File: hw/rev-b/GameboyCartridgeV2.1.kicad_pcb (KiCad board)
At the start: 6 copper layers, 52.8 x 61.2 mm, 148 parts, among them J1 USB_C_Receptacle_USB2.0, J2 Micro_SD_Card_Det2, J4 Conn_01x06, J5 CartBus, Q1 CJ2302, Q101 SIA975DJ-T1-GE3, Q102 2N7002, SW1 SW_Push, SW2 SW_Push, U1 USBLC6-2P6, U101 TPS2116DRLR, U102 TPS2553DBVR, U103 TPS63802DLAR, U104 ESP32-C3-MINI-1U-N4, U105 SN74LVC1G125DBVR, U106 SN74LVC3G34DCTR, U107 CH334P, U108 TLV3012BIDBVR, U109 TLV431BIDBZR, U2 W25Q16JVSSIQ, U3 RP2350_80QFN, U4 W956A8MBYA5I, U5 MCP79510, U6 AP2112K-3.3, U7 TXB0108PW, Y1 12MHz, Y101 12MHz 10pF 10ppm, Y2 32.768kHz

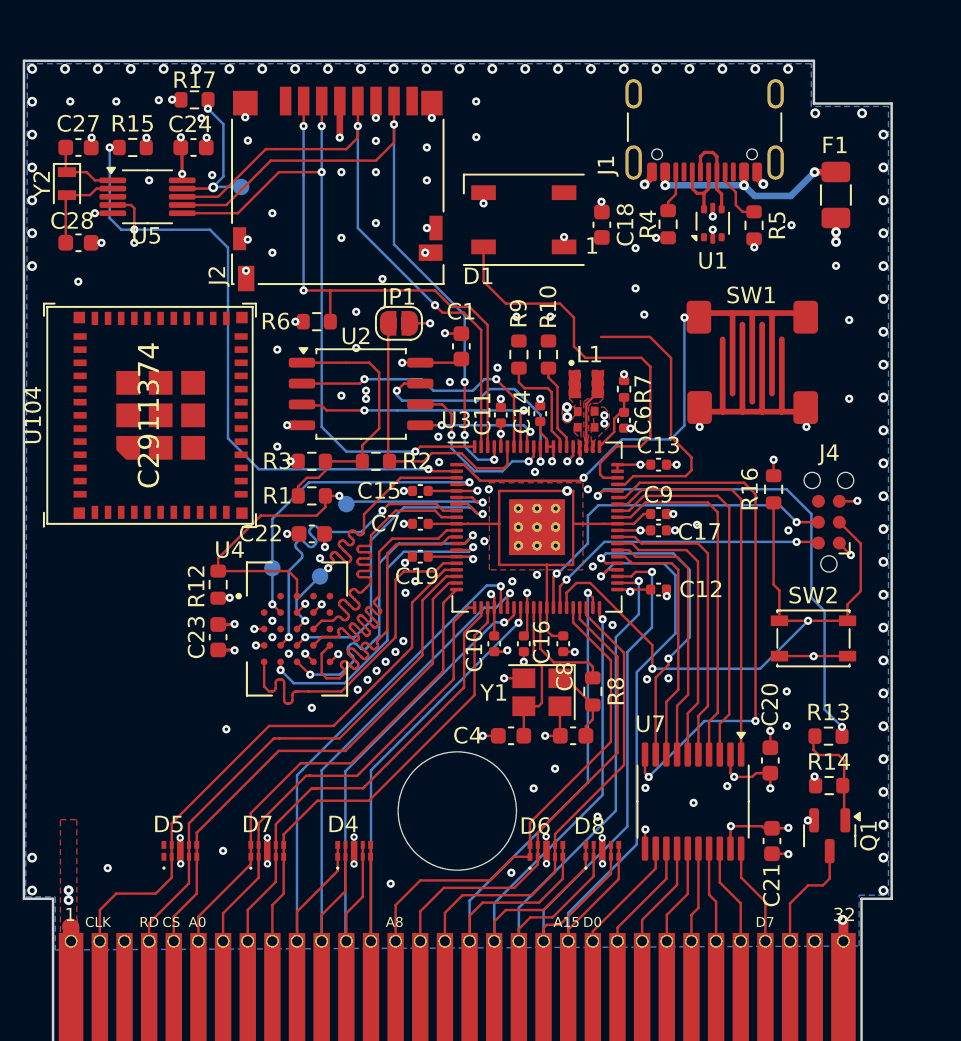
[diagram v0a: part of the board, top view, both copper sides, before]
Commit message: layout: rip 41 slow Croco signal nets off the outer layers for inner-layer re-route (core HyperRAM/QSPI/USB/xtal/power routing kept)
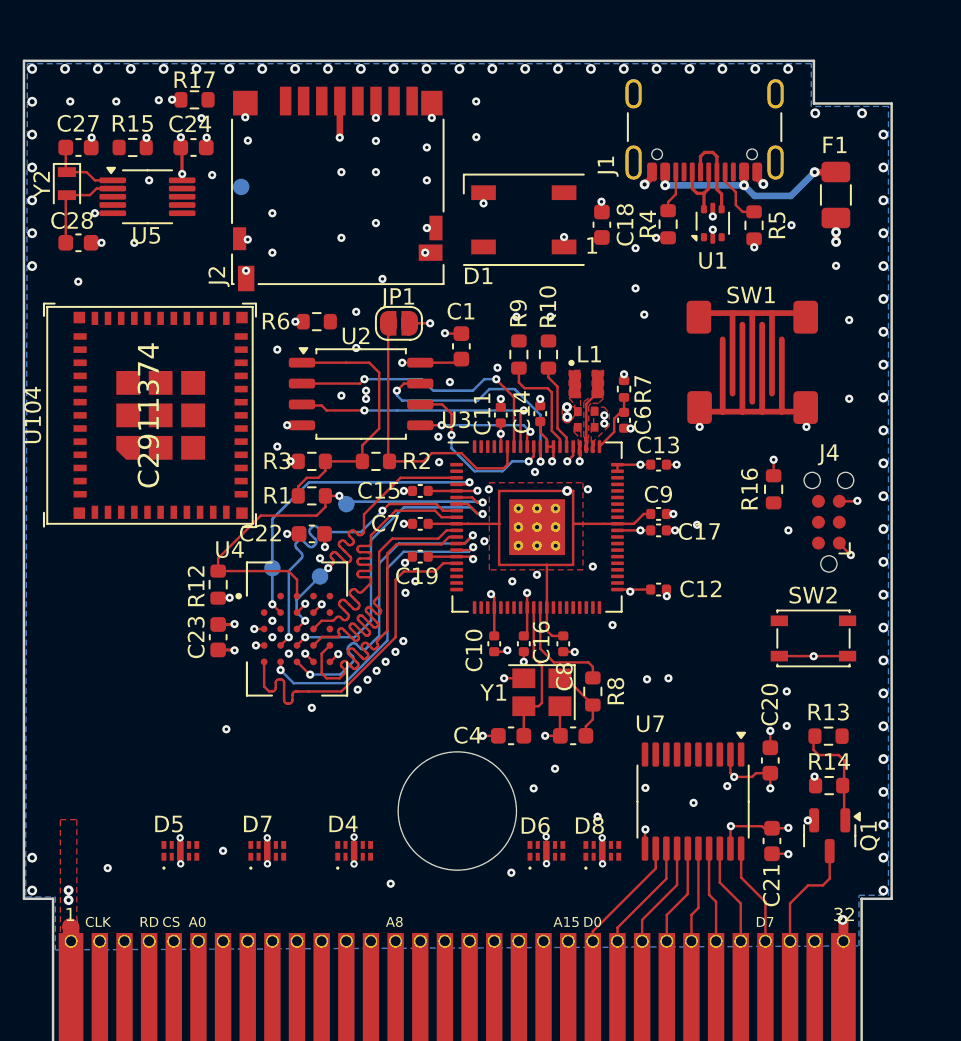
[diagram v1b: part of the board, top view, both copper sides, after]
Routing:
- net RTC_CS: track 41.9 -> 0.00 mm, vias 3 -> 0
- net SPI_MISO: track 41.3 -> 0.00 mm, vias 4 -> 0
- net SPI_MOSI: track 39.4 -> 0.00 mm, vias 3 -> 0
- net GB_A15: track 38.4 -> 0.00 mm, vias 1 -> 0
- net RST: track 38.4 -> 0.00 mm, vias 2 -> 0
- net SPI_CLK: track 37.8 -> 0.00 mm, vias 2 -> 0
- net GB_CLK: track 35.7 -> 0.00 mm
- net GB_A4: track 35.5 -> 0.00 mm, vias 1 -> 0
- net GB_A14: track 35.4 -> 0.00 mm, vias 1 -> 0
- net GB_A11: track 35.4 -> 0.00 mm, vias 1 -> 0
- net GB_A13: track 34.8 -> 0.00 mm, vias 1 -> 0
- net GB_A5: track 33.7 -> 0.00 mm, vias 1 -> 0
- net SD_CARD_CS: track 32.9 -> 0.00 mm, vias 2 -> 0
- net GB_RD: track 32.6 -> 0.00 mm
- net GB_A12: track 32.6 -> 0.00 mm, vias 1 -> 0
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
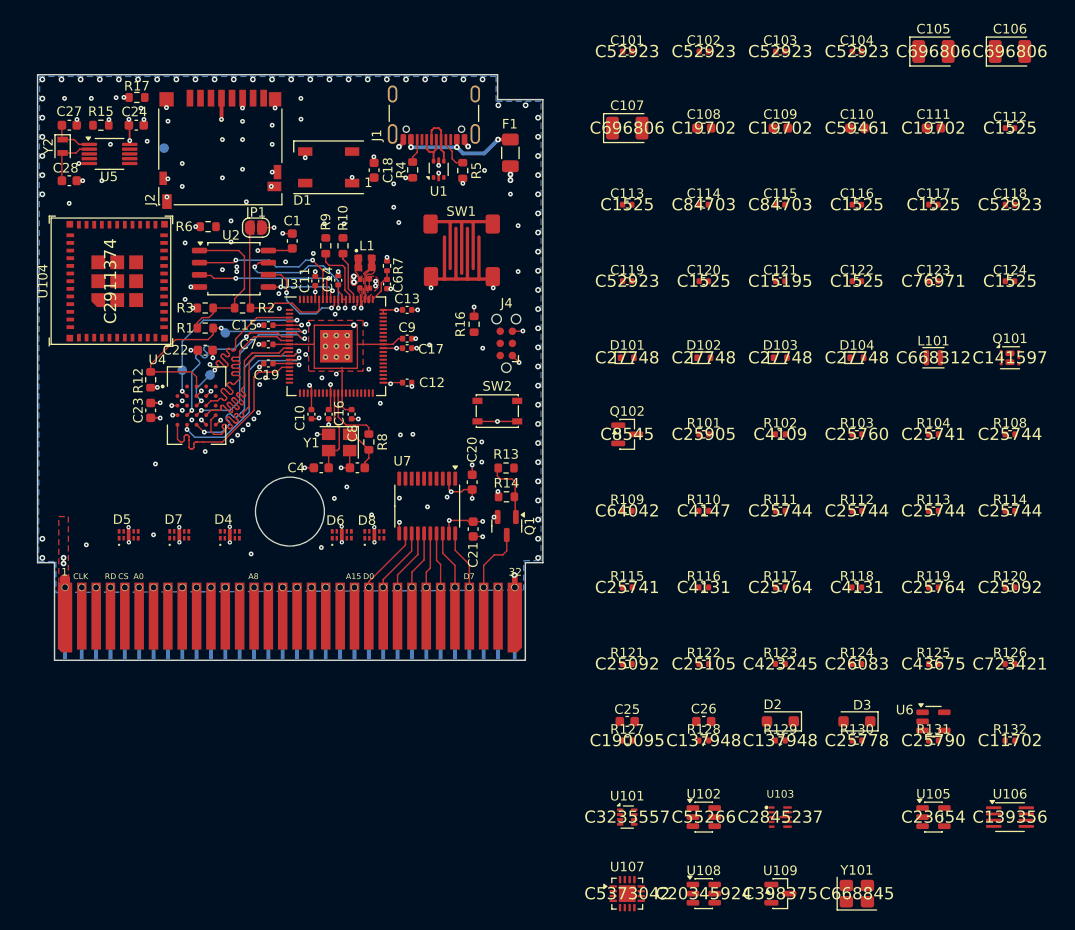
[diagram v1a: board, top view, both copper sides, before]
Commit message: layout: all parts placed on the 6-layer board (groups + autoplace), D1 restored, logbook
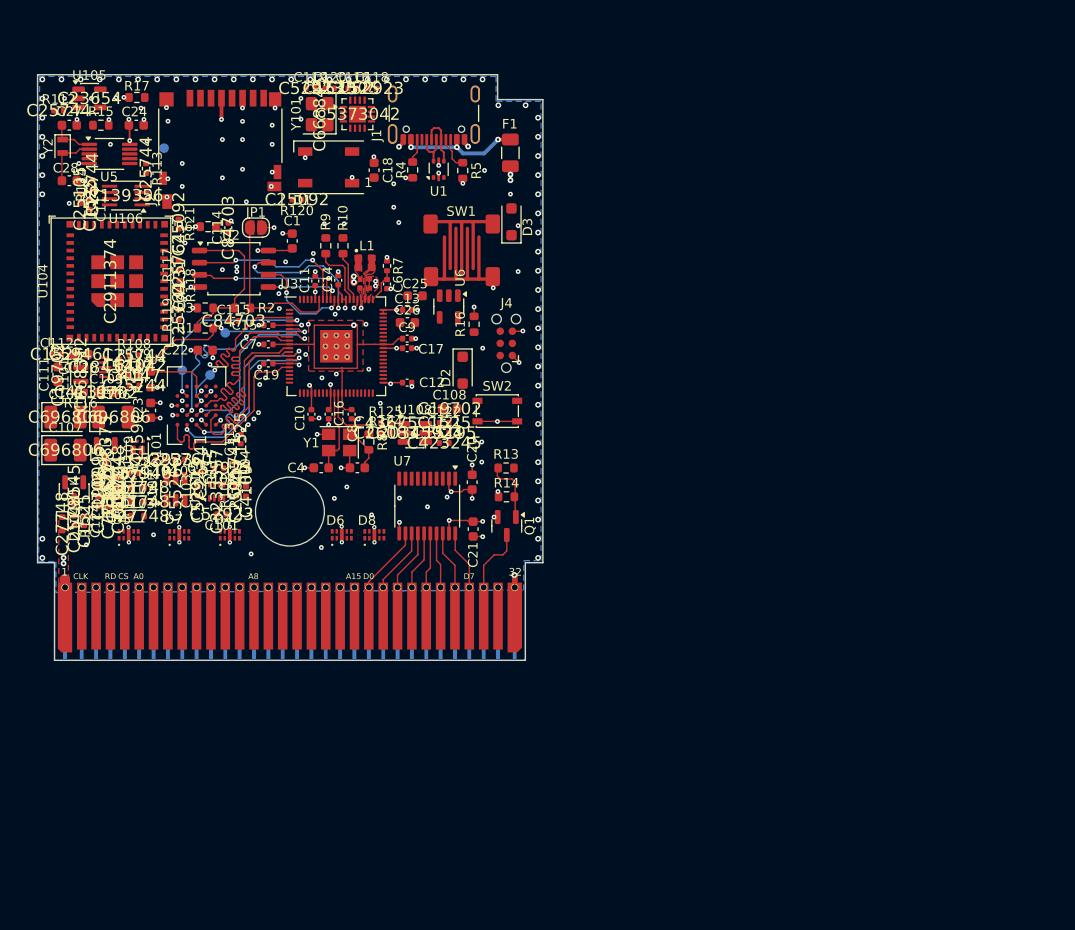
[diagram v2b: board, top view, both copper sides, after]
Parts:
- moved U105 115.8 mm to (118.8, 64.9)
- moved U106 112.9 mm to (122.6, 75.1), turned to 180 degrees
- moved C112 102.4 mm to (115.4, 91.6)
- moved R114 101.8 mm to (119.1, 73.9), turned to 90 degrees
- moved C106 101.2 mm to (121.3, 98.2)
- moved C124 99.9 mm to (118.3, 109.1), turned to -90 degrees
- moved Y101 98.9 mm to (142.9, 66.6), turned to 90 degrees
- moved R132 98.5 mm to (119.7, 107.1), turned to -90 degrees
- moved C105 98.4 mm to (116.3, 98.2)
- moved R126 95.8 mm to (120.8, 107.1), turned to -90 degrees
- moved C111 95.1 mm to (115.5, 93.8), turned to 90 degrees
- moved R112 93.3 mm to (115.6, 66.2)
- moved R131 92.7 mm to (117.2, 109.1), turned to -90 degrees
- moved R108 91.9 mm to (123.5, 91.8)
- moved Q101 91.7 mm to (123.8, 101.7), turned to -90 degrees
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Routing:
- net GND: track 49.6 -> 49.0 mm, vias 198 -> 194
- net +3V3: track 46.4 -> 45.8 mm

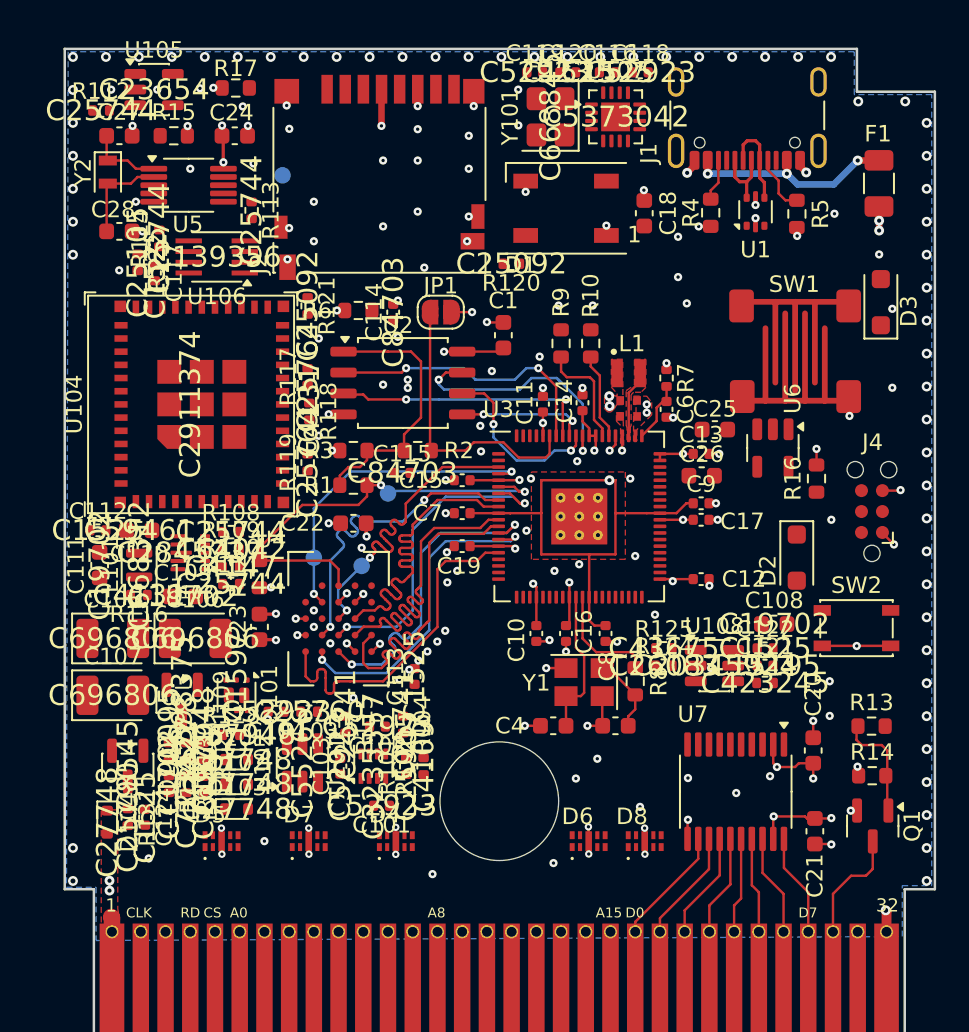
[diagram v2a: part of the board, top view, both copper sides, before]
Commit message: routing pass 1: Freerouting 2.5 on 6 layers (rules 0.15/0.15, vias 0.5/0.2, Power class 0.35), own SES importer (KiCad's fails silently); unconnected 293 -> 41
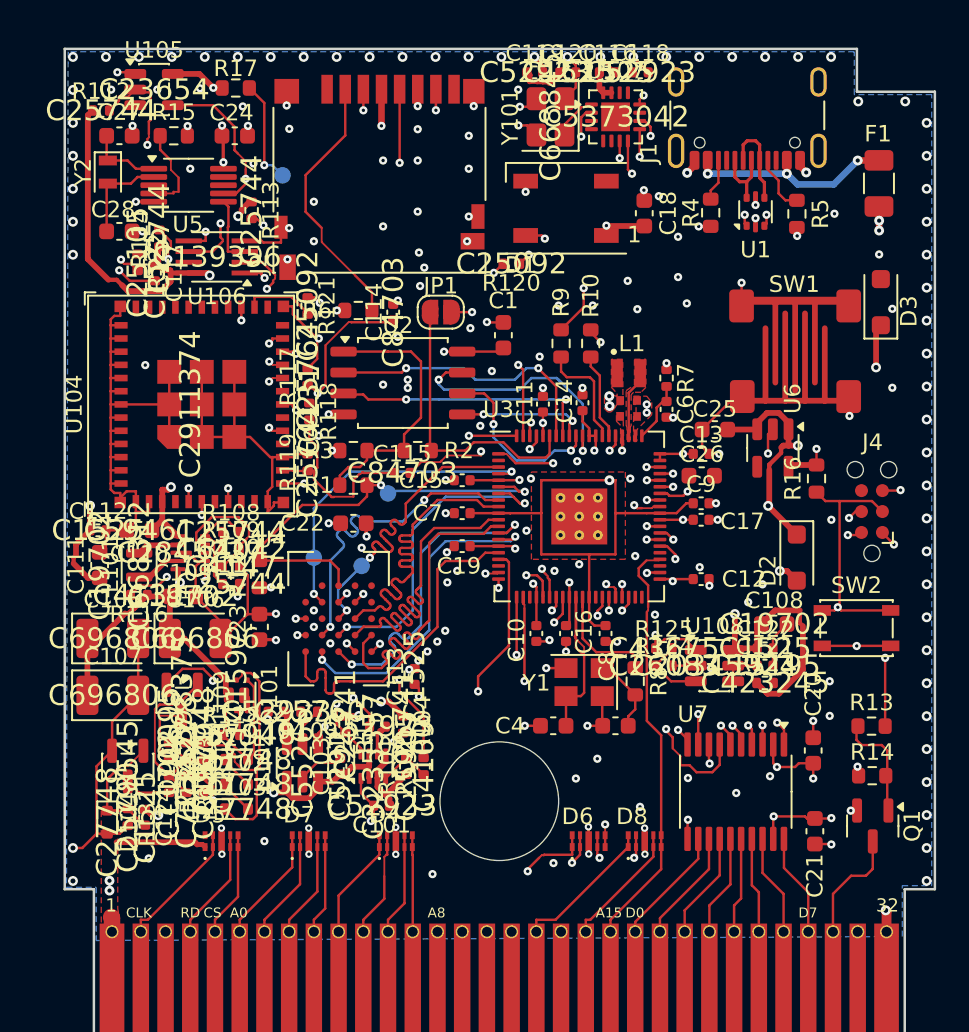
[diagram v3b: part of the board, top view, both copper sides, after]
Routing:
- net GND: track 49.0 -> 193.3 mm, vias 194 -> 196
- net /Radio/+3V3_RF: track 0.00 -> 81.5 mm, vias 0 -> 6
- net VRES: track 0.00 -> 70.1 mm, vias 0 -> 2
- net SPI_MISO: track 0.00 -> 48.1 mm, vias 0 -> 3
- net GB_CLK: track 0.00 -> 44.0 mm, vias 0 -> 1
- net GB_CS: track 0.00 -> 36.2 mm, vias 0 -> 1
- net GB_A0: track 0.00 -> 35.4 mm, vias 0 -> 1
- net GB_A4: track 0.00 -> 35.4 mm, vias 0 -> 1
- net GB_A5: track 0.00 -> 34.9 mm, vias 0 -> 1
- net SPI_CLK: track 0.00 -> 34.9 mm, vias 0 -> 3
- net /Radio/RF_EN: track 0.00 -> 34.0 mm, vias 0 -> 2
- net GB_A1: track 0.00 -> 33.4 mm, vias 0 -> 1
- net GB_A2: track 0.00 -> 32.8 mm, vias 0 -> 1
- net GB_A8: track 0.00 -> 32.5 mm, vias 0 -> 2
- net GB_A6: track 0.00 -> 30.9 mm, vias 0 -> 1
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
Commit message: routing pass 2 on the remaining connections; unconnected 41 -> 27
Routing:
- net GB_RD: track 6.86 -> 47.6 mm, vias 0 -> 1
- net GB_A14: track 7.72 -> 40.0 mm, vias 0 -> 1
- net GB_A11: track 11.3 -> 31.8 mm, vias 1 -> 3
- net SWCLK: track 0.92 -> 19.3 mm, vias 1 -> 2
- net SWDIO: track 2.14 -> 19.6 mm
- net SD_CARD_CS: track 16.9 -> 32.4 mm, vias 1 -> 3
- net /Radio/ESP_SCK_BUF: track 0.00 -> 14.5 mm, vias 0 -> 2
- net USB_D_prot-: track 0.72 -> 11.8 mm, vias 1 -> 2
- net GND: track 193.3 -> 202.6 mm
- net SPI_CLK: track 34.9 -> 44.0 mm, vias 3 -> 4
- net Net-(U5-MFP): track 6.42 -> 13.5 mm, vias 1 -> 2
- net /Radio/REG_CCN: track 0.00 -> 6.19 mm, vias 0 -> 2
- net +3V3: track 57.8 -> 59.9 mm, vias 31 -> 32
- net Net-(U3-XOUT): track 7.44 -> 8.05 mm

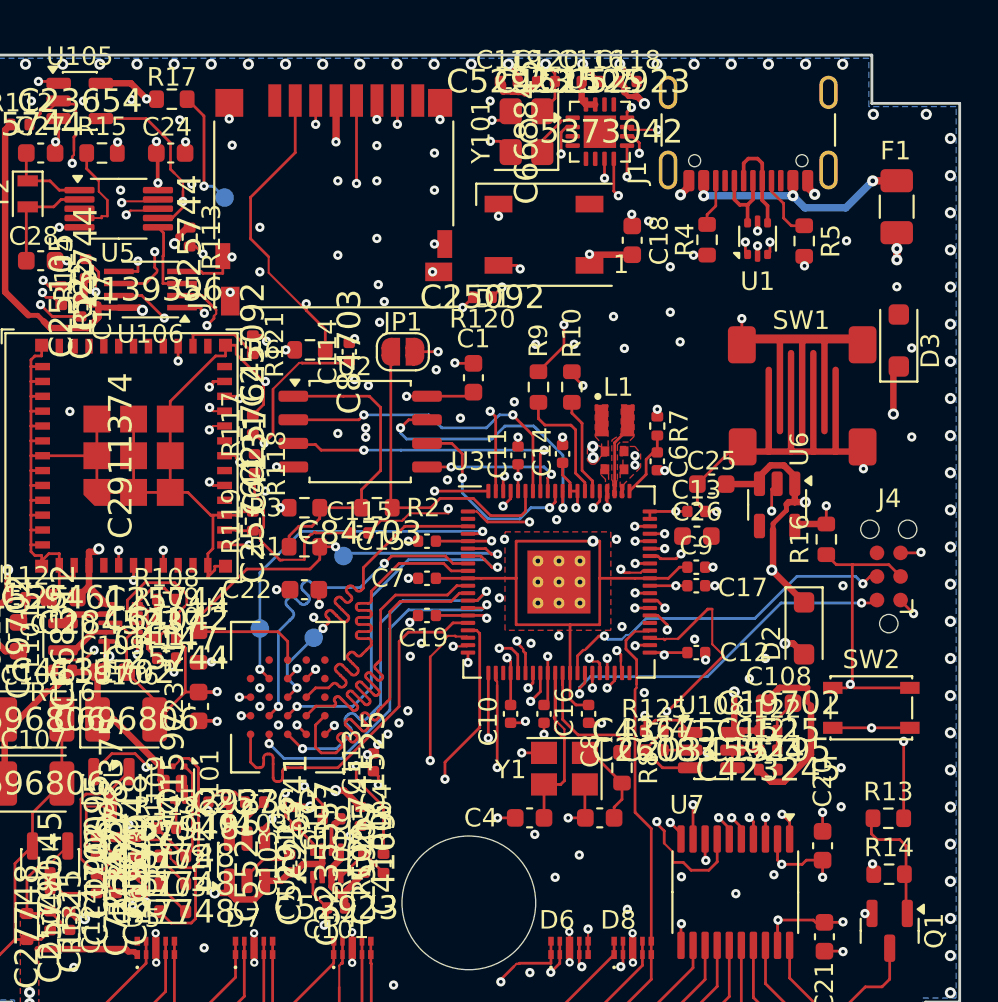
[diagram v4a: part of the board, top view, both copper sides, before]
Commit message: routing: own inner-layer finisher (A* on In2/In3, via legality on all signal layers, reuses existing vias), BUTTON re-routed off the SW1 contact pattern; unconnected 27 -> 15
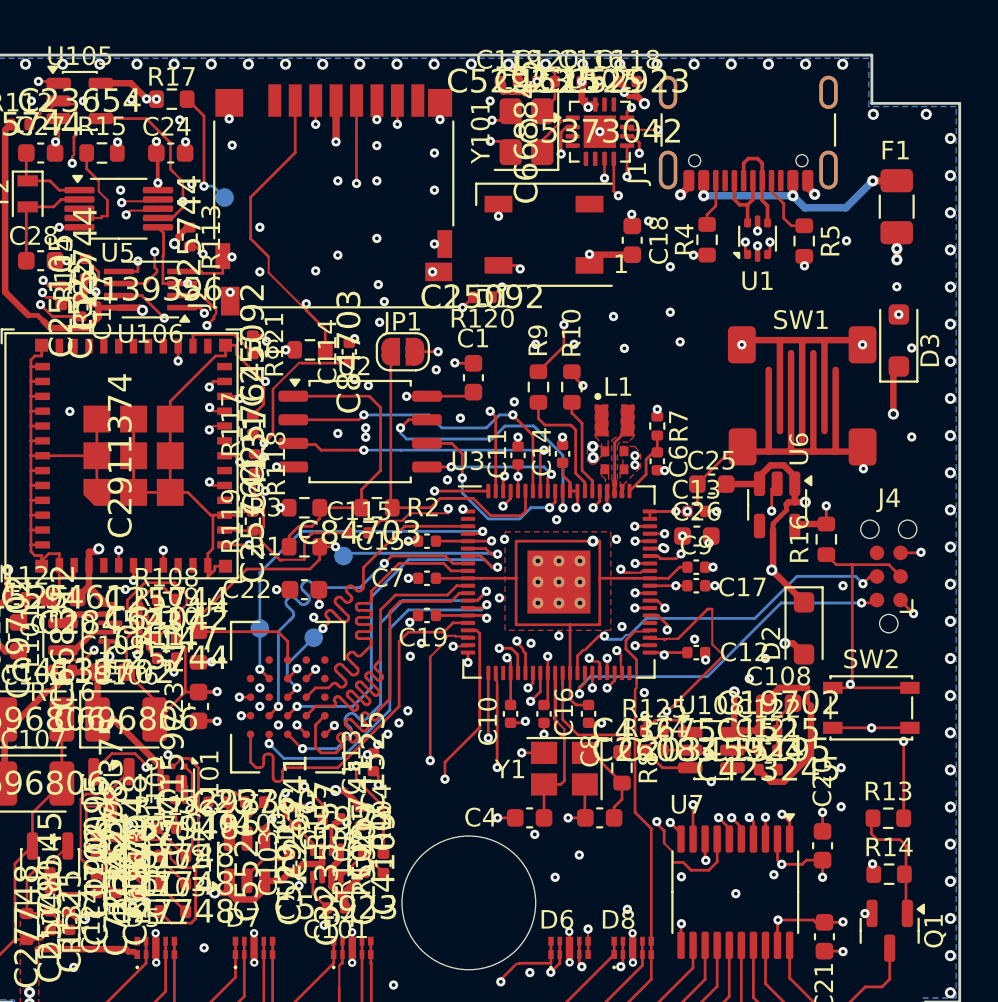
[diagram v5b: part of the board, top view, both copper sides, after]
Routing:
- net VCC: track 29.9 -> 65.9 mm, vias 5 -> 10
- net GBBUS_EN: track 1.92 -> 20.1 mm, vias 2 -> 4
- net +3V3: track 59.9 -> 77.0 mm, vias 32 -> 40
- net SPI_MOSI: track 30.8 -> 38.3 mm, vias 2 -> 4
- net GND: track 202.6 -> 207.6 mm, vias 196 -> 199
- net VBUS: track 7.41 -> 10.8 mm, vias 3 -> 4
- net /Radio/VMUX: track 17.8 -> 20.9 mm, vias 2 -> 3
- net BUTTON: track 28.5 -> 25.5 mm, vias 2 -> 3
